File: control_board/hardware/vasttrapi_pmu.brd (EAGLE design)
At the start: 52.4 x 29.2 mm, 21 parts, among them J2 3p-2.54, U1 TINY85-20-DIP, U2 RELAY, Y1 12MHZ

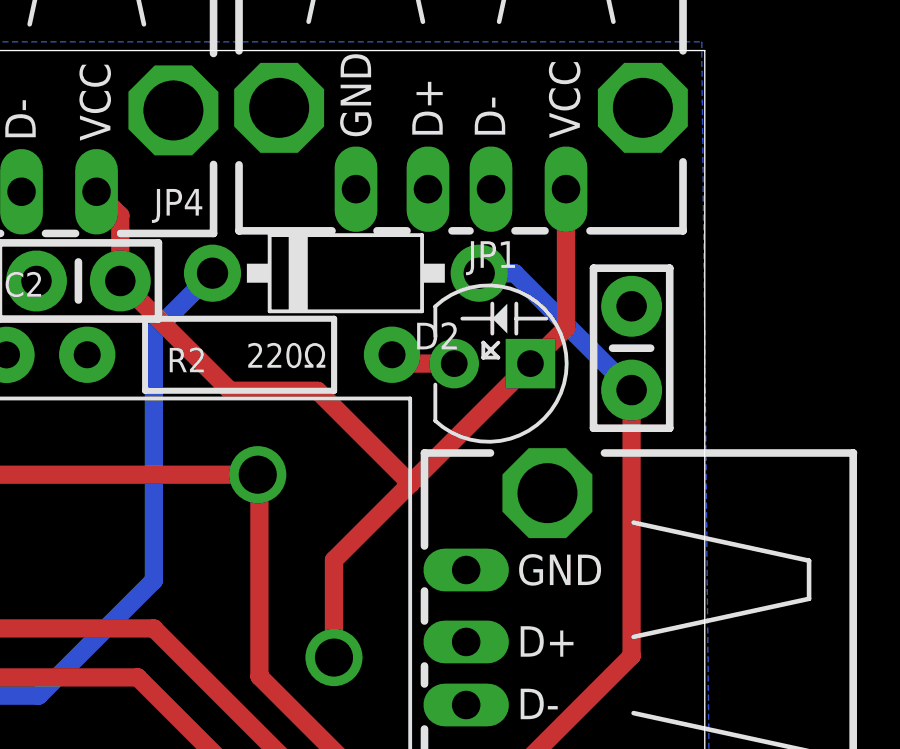
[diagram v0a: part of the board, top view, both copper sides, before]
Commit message: led position fix
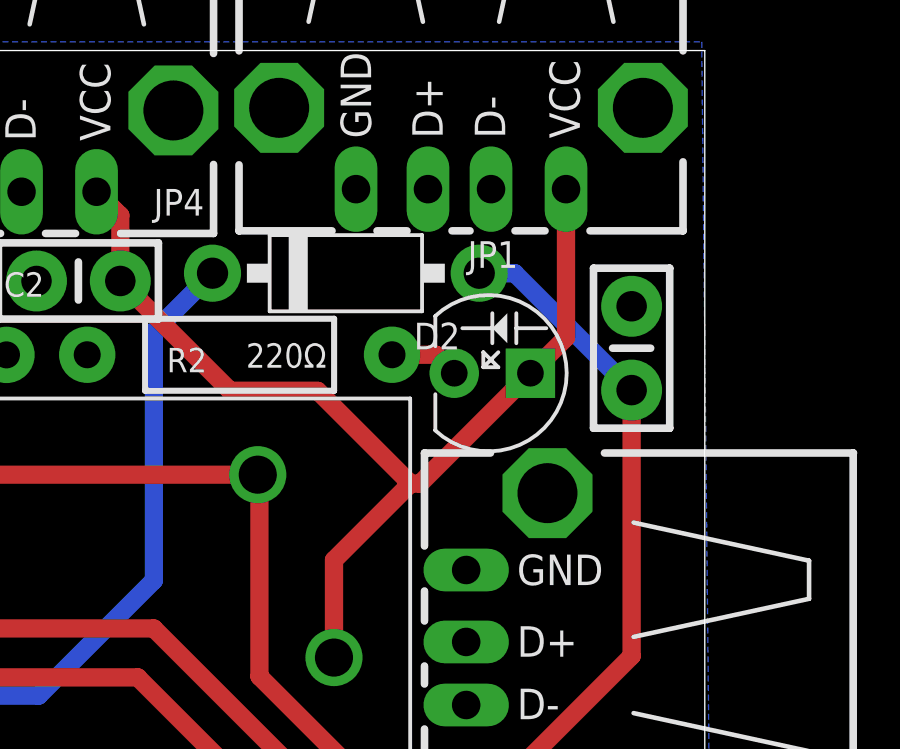
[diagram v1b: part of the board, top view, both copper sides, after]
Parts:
- moved D1 0.32 mm to (67.3, 42.8)
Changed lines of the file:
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@@
 <attribute name="VALUE" x="22.113240625" y="40.406321875" size="0.889" layer="27" ratio="11" rot="R270"/>
 </element>
-<element name="D1" library="Seeed-OPL-Diode" package="LED2-2.54-D5.0MM" value="G502DC" x="67.29" y="43.0722" smashed="yes" rot="R180">
-<attribute name="MPN" value="G502DC" x="67.29" y="43.0722" size="1.778" layer="27" rot="R180" display="off"/>
-<attribute name="NAME" x="69.195" y="39.8972" size="0.889" layer="27" ratio="11" rot="R180"/>
-<attribute name="VALUE" x="65.2326" y="45.3582" size="0.635" layer="27" ratio="10" rot="R180"/>
+<element name="D1" library="Seeed-OPL-Diode" package="LED2-2.54-D5.0MM" value="G502DC" x="67.29" y="42.752159375" smashed="yes" rot="R180">
+<attribute name="MPN" value="G502DC" x="67.29" y="42.752159375" size="1.778" layer="27" rot="R180" display="off"/>
+<attribute name="NAME" x="69.195" y="39.577159375" size="0.889" layer="27" ratio="11" rot="R180"/>
+<attribute name="VALUE" x="65.2326" y="45.038159375" size="0.635" layer="27" ratio="10" rot="R180"/>
 </element>
 <element name="R2" library="SparkFun-Passives" package="AXIAL-0.4" value="220Ω" x="58.8664" y="43.3678" smashed="yes" rot="R180">
@@
 <contactref element="D1" pad="+"/>
 <wire x1="62.0114" y1="33.274" x2="62.0114" y2="36.5238" width="0.6096" layer="1"/>
-<wire x1="64.5598" y1="39.0722" x2="68.5598" y2="43.0722" width="0.6096" layer="1"/>
 <contactref element="JP4" pad="1"/>
 <contactref element="C5" pad="2"/>
-<wire x1="64.5598" y1="39.0722" x2="62.0114" y2="36.5238" width="0.6096" layer="1"/>
-<wire x1="69.7462" y1="48.888" x2="69.7462" y2="44.2586" width="0.6096" layer="1"/>
-<wire x1="69.7462" y1="44.2586" x2="68.5598" y2="43.0722" width="0.6096" layer="1"/>
+<wire x1="62.0114" y1="36.5238" x2="64.5598" y2="39.0722" width="0.6096" layer="1"/>
 <wire x1="64.5598" y1="39.0722" x2="61.468" y2="42.164" width="0.6096" layer="1"/>
 <wire x1="58.552078125" y1="42.164" x2="54.8894" y2="45.826678125" width="0.6096" layer="1"/>
@@
 <wire x1="54.8894" y1="45.826678125" x2="54.8894" y2="48.0086" width="0.6096" layer="1"/>
 <wire x1="54.8894" y1="48.0086" x2="54.0968" y2="48.8012" width="0.6096" layer="1"/>
+<wire x1="64.5598" y1="39.0722" x2="64.879840625" y2="39.0722" width="0.6096" layer="1"/>
+<wire x1="64.879840625" y1="39.0722" x2="68.5598" y2="42.752159375" width="0.6096" layer="1"/>
+<wire x1="68.5598" y1="42.752159375" x2="69.7462" y2="43.938559375" width="0.6096" layer="1"/>
+<wire x1="69.7462" y1="43.938559375" x2="69.7462" y2="48.888" width="0.6096" layer="1"/>
 </signal>
 <signal name="D-">
@@
 <contactref element="D1" pad="-"/>
 <contactref element="R2" pad="P$1"/>
-<wire x1="66.0202" y1="43.0722" x2="64.242" y2="43.0722" width="0.6096" layer="1"/>
-<wire x1="64.242" y1="43.0722" x2="63.9464" y2="43.3678" width="0.6096" layer="1"/>
+<wire x1="63.9464" y1="43.3678" x2="65.404559375" y2="43.3678" width="0.6096" layer="1"/>
+<wire x1="65.404559375" y1="43.3678" x2="66.0202" y2="42.752159375" width="0.6096" layer="1"/>
 </signal>
 <signal name="N$3">
